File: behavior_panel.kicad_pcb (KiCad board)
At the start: 2 copper layers, 64 x 119 mm, 85 parts, among them J1 Conn_01x04, J17 Conn_01x05_Pin, J18 Conn_01x03_Pin, J19 Conn_01x05_Pin, J2 Conn_01x04, J20 Conn_01x05_Pin, J21 Conn_01x03_Pin, J22 Conn_01x05_Pin, J23 Conn_01x03_Pin, J24 Conn_01x03_Pin, J3 Conn_01x04, J5 Conn_01x04, Q1 N MOSFET, Q2 Q_NPN_BCE, Q3 N MOSFET, Q4 Q_NPN_BCE, Q5 N MOSFET, Q6 Q_NPN_BCE, Q7 N MOSFET, Q8 Q_NPN_BCE, U1 LM317_3PinPackage, U2 LM317_3PinPackage, U3 LM2902

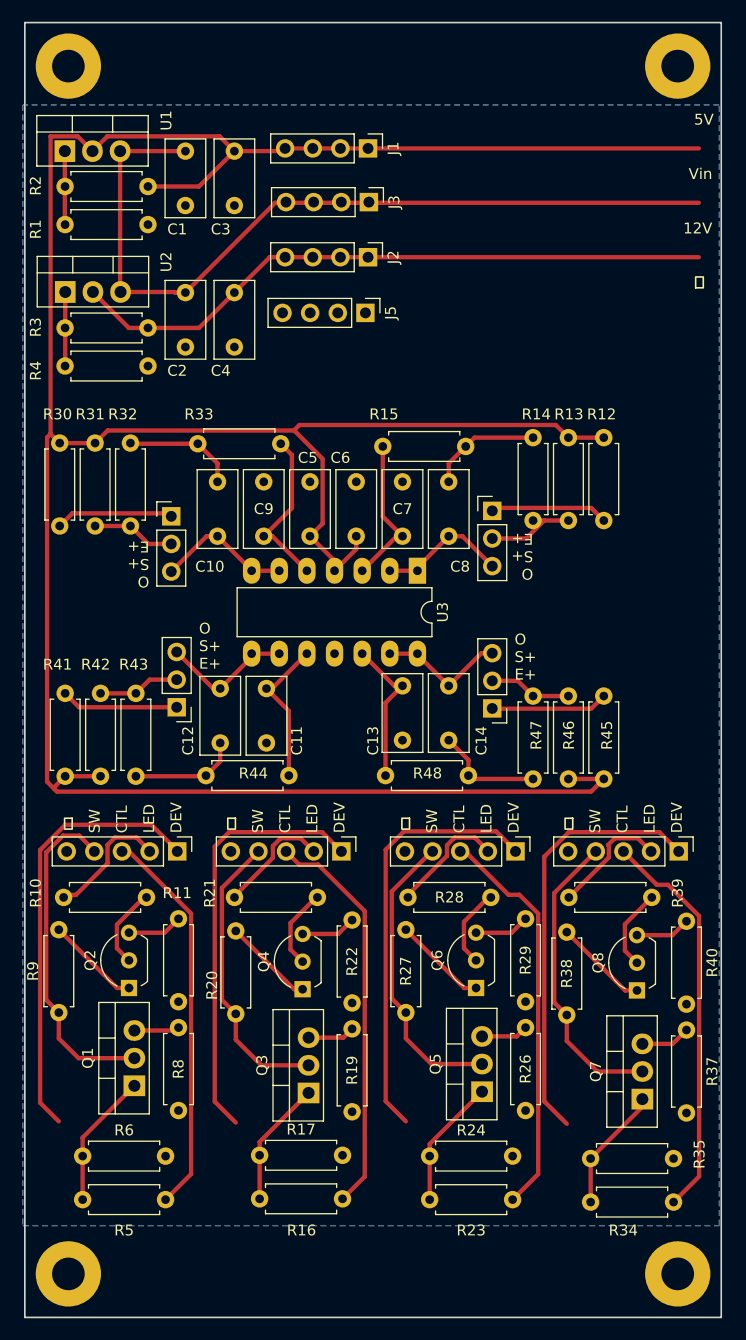
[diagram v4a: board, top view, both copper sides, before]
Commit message: Release of V2 of behavior panel
* LED indicators should now be working
* Slightly narrower board
* Added recommended values for footprints
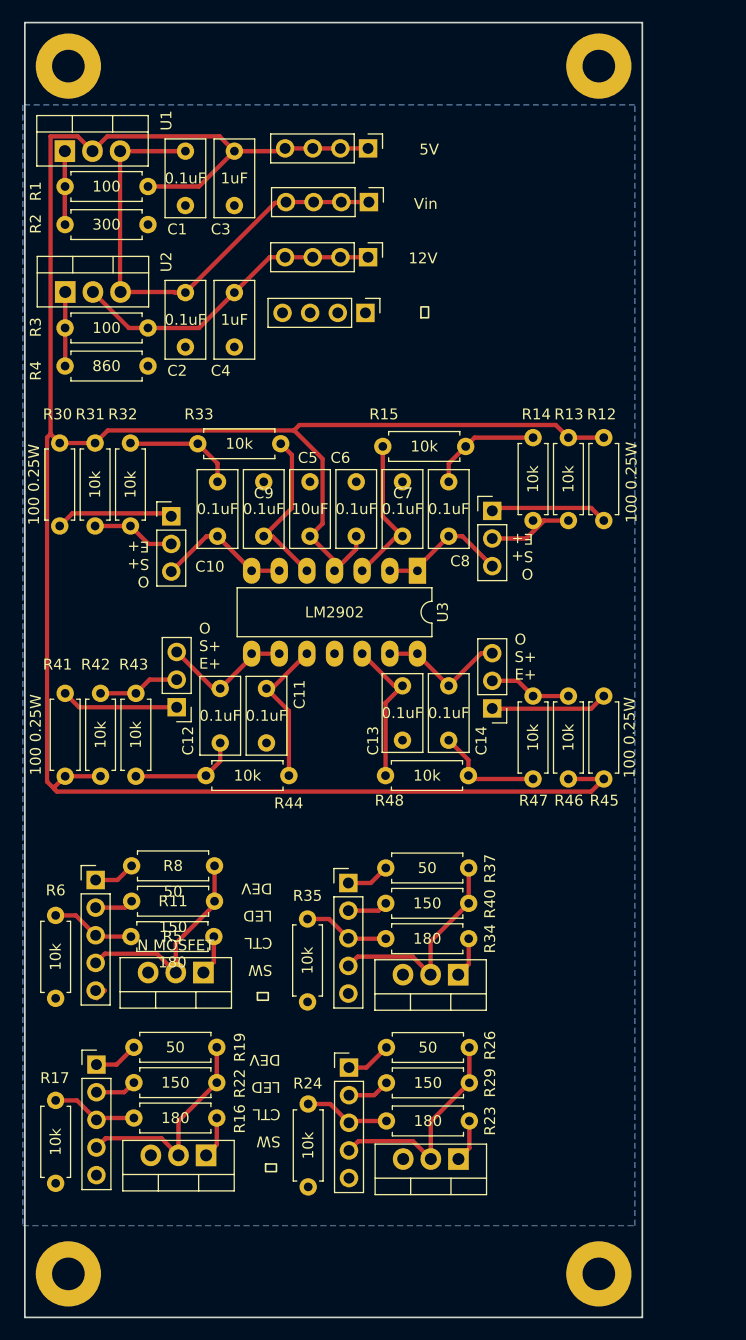
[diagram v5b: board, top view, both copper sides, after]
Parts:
- removed Q2, Q4, Q6, Q8: Q_NPN_BCE, Package_TO_SOT_THT:TO-92L_Inline_Wide
- removed R10, R20, R21, R27, R28, R38, R39, R9: 10k, Resistor_THT:R_Axial_DIN0207_L6.3mm_D2.5mm_P7.62mm_Horizontal
- R11, R22, R29, R40: value 10k -> 150
- R16, R23, R34, R5: value 2.2k -> 180
- moved R34 35.8 mm to (133.2, 114.2), turned to 0 degrees
- moved R35 34.1 mm to (126.0, 112.4), turned to -90 degrees
- moved R37 31.4 mm to (133.2, 107.7), turned to 0 degrees
- moved J22 30.5 mm to (129.7, 109.1), turned to 0 degrees
- moved J19 29.8 mm to (106.6, 125.8), turned to 0 degrees
- moved R40 27.7 mm to (133.2, 110.9), turned to 0 degrees
- moved J20 25.1 mm to (129.8, 126.0), turned to 0 degrees
- moved R22 25.0 mm to (110.0, 127.4), turned to 0 degrees
- moved R5 24.4 mm to (109.8, 114.0), turned to 0 degrees
- moved R6 22.3 mm to (102.8, 112.1), turned to -90 degrees
- moved R16 20.6 mm to (110.0, 130.7), turned to 0 degrees
- moved Q7 20.4 mm to (139.8, 117.5), turned to 180 degrees
- moved R19 20.1 mm to (110.0, 124.2), turned to 0 degrees
- moved R29 19.8 mm to (133.2, 127.4), turned to 0 degrees
- moved R17 19.4 mm to (102.8, 129.1), turned to -90 degrees
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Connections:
- J17 pad 4: /power control/device in -> /power control/switch out
- J19 pad 4: /power control2/device in -> /power control2/switch out
- J20 pad 4: /power control3/device in -> /power control3/switch out
- J22 pad 4: /power control4/device in -> /power control4/switch out
- Q1 pad 2: /power control/device in -> /power control/switch out
- Q1 pad 3: Net-(Q1-S) -> GND
- Q3 pad 2: /power control2/device in -> /power control2/switch out
- Q3 pad 3: Net-(Q3-S) -> GND
- Q5 pad 2: /power control3/device in -> /power control3/switch out
- Q5 pad 3: Net-(Q5-S) -> GND
- Q7 pad 2: /power control4/device in -> /power control4/switch out
- Q7 pad 3: Net-(Q7-S) -> GND
- R11 pad 1: Net-(Q2-E) -> /power control/LED in
- R11 pad 2: GND -> /power control/switch out
- R17 pad 1: Net-(Q3-G) -> /power control2/CTL
- R19 pad 1: Net-(Q3-S) -> /power control2/device in
- R19 pad 2: GND -> /power control2/switch out
- R22 pad 1: Net-(Q4-E) -> /power control2/LED in
- R22 pad 2: GND -> /power control2/switch out
- R24 pad 1: Net-(Q5-G) -> /power control3/CTL
- R26 pad 1: Net-(Q5-S) -> /power control3/device in
- R26 pad 2: GND -> /power control3/switch out
- R29 pad 1: Net-(Q6-E) -> /power control3/LED in
- R29 pad 2: GND -> /power control3/switch out
- R35 pad 1: Net-(Q7-G) -> /power control4/CTL
- R37 pad 1: Net-(Q7-S) -> /power control4/device in
- R37 pad 2: GND -> /power control4/switch out
- R40 pad 1: Net-(Q8-E) -> /power control4/LED in
- R40 pad 2: GND -> /power control4/switch out
- R6 pad 1: Net-(Q1-G) -> /power control/CTL
- R8 pad 1: Net-(Q1-S) -> /power control/device in
- R8 pad 2: GND -> /power control/switch out
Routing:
- net /power control/device in: track 71.1 -> 3.84 mm
- net /power control4/device in: track 67.0 -> 4.01 mm
- net /power control3/device in: track 66.4 -> 4.20 mm
- net /power control2/device in: track 66.0 -> 4.10 mm
- net 5V: track 262.0 -> 231.5 mm
- net 12V: track 59.7 -> 29.3 mm
- net VIN: track 75.5 -> 45.1 mm
- net /power control3/CTL: track 36.8 -> 7.98 mm
- net /power control2/CTL: track 36.8 -> 8.00 mm
- net /power control4/CTL: track 36.7 -> 7.94 mm
- net /power control/CTL: track 36.0 -> 8.08 mm
- net /power control3/switch out: track 0.00 -> 20.3 mm
- net /power control2/switch out: track 0.00 -> 19.9 mm
- net /power control4/switch out: track 0.00 -> 19.9 mm
- net /power control/switch out: track 0.00 -> 19.7 mm
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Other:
- board size 64 x 119 mm -> 56.8 x 119 mm
- board text added: "LBHB master behavior circuit (9/10/2024) Designed by Brad Buran & Satya Parida"
- board text removed: "LBHB master behavior circuit (4/16/2024) Designed by Brad Buran & Satya Parida"

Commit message: Add more ground pins. Fix labels.
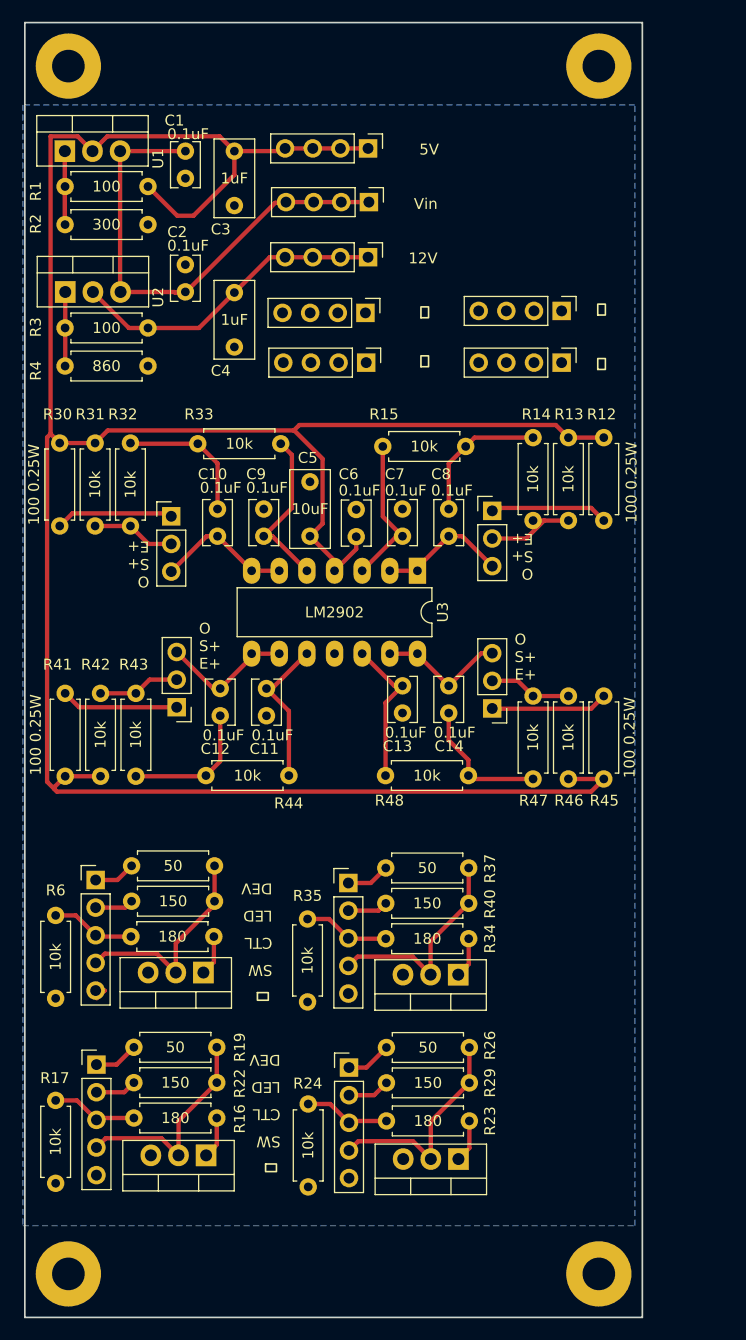
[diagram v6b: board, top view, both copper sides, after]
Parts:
- added J4: Conn_01x04, Connector_PinHeader_2.54mm:PinHeader_1x04_P2.54mm_Vertical, F.Cu at (131.4, 61.2)
- added J6: Conn_01x04, Connector_PinHeader_2.54mm:PinHeader_1x04_P2.54mm_Vertical, F.Cu at (149.3, 61.2)
- added J7: Conn_01x04, Connector_PinHeader_2.54mm:PinHeader_1x04_P2.54mm_Vertical, F.Cu at (149.3, 56.5)
- C1, C10, C11, C12, C13, C14, C2, C6, C7, C8, C9: footprint Capacitor_THT:C_Rect_L7.0mm_W3.5mm_P5.00mm -> Capacitor_THT:C_Rect_L4.0mm_W2.5mm_P2.50mm
- moved C6 2.55 mm to (130.5, 74.8)
- moved C2 0.07 mm to (114.8, 54.8), turned to 90 degrees
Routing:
- net 5V: track 231.5 -> 235.0 mm
- net Net-(C14-Pad2): track 10.1 -> 12.6 mm
- net Net-(C12-Pad2): track 10.0 -> 12.5 mm
- net Net-(C10-Pad2): track 10.5 -> 13.0 mm
- net Net-(C8-Pad2): track 10.4 -> 12.9 mm
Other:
- board text added: "LBHB master behavior circuit (2/11/2025) Designed by Brad Buran & Satya Parida"
- board text removed: "LBHB master behavior circuit (9/10/2024) Designed by Brad Buran & Satya Parida"
